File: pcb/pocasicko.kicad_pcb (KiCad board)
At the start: 2 copper layers, 100 x 88 mm, 65 parts, among them J1 SMA, J2 Header_SMD_1x05, J3 FPC24, J4 Header_SMD_1x03, Q1 AO3400A, SW1 SW_Push, SW2 A, SW3 B, SW4 C, SW5 D, U1 CMWX1ZZABZ-091, U2 BME680, U3 MP28200, U4 LM66100

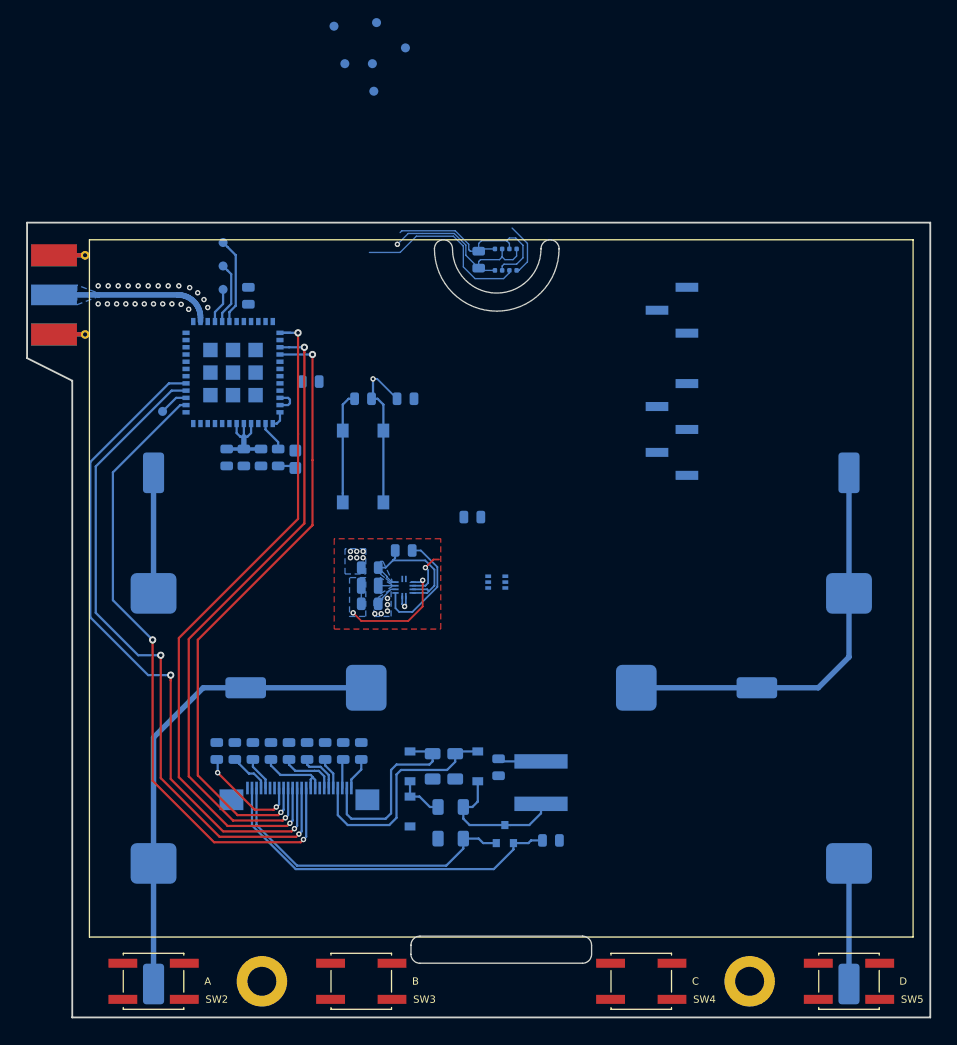
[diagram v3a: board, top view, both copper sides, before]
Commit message: Rotate the center cell diagonally
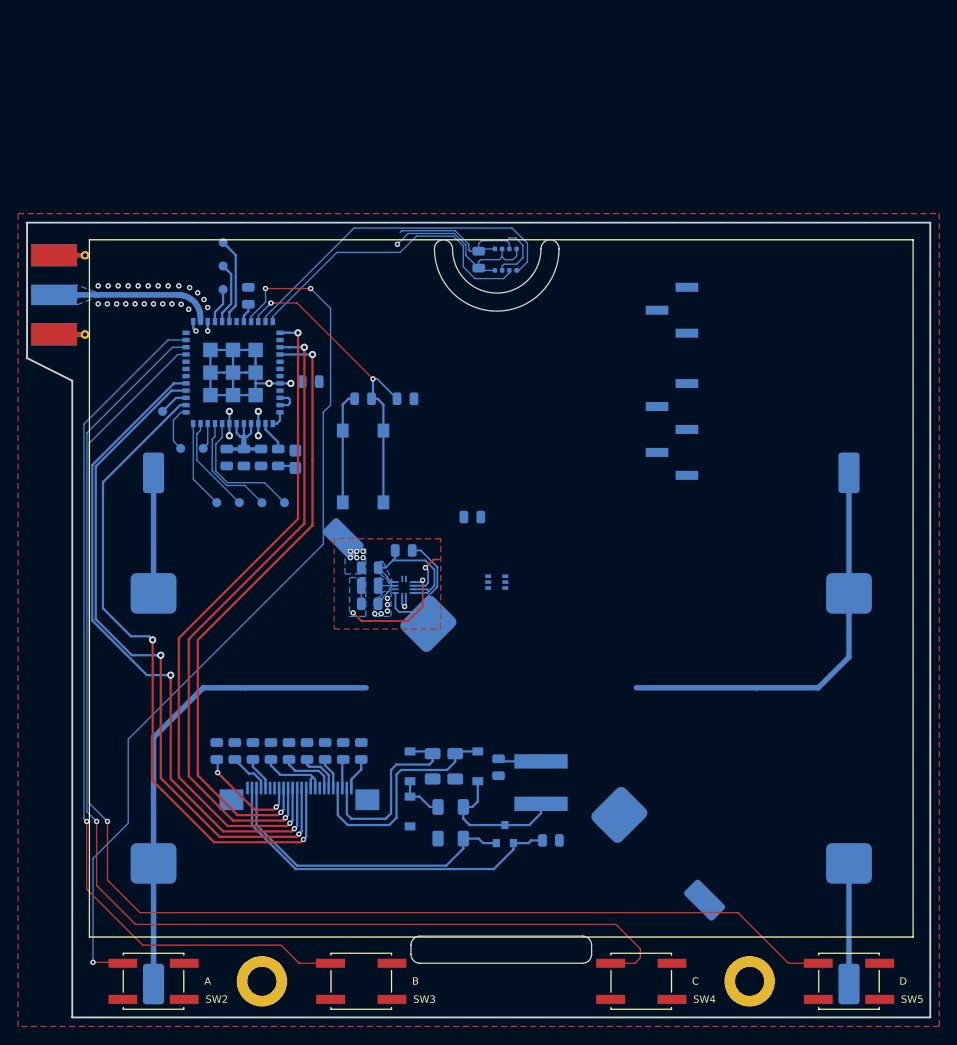
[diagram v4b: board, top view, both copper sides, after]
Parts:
- moved TP6 54.1 mm to (128.5, 81.0)
- moved TP9 53.6 mm to (123.5, 81.0)
- moved TP7 53.4 mm to (126.0, 81.0)
- moved TP5 48.8 mm to (121.0, 81.0)
- moved TP8 46.5 mm to (119.5, 75.0)
- moved TP4 46.3 mm to (117.0, 75.0)
- moved BT2 4.30 mm to (155.0, 105.0), turned to -45 degrees
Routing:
- net /BUTTON_D: track 0.00 -> 146.5 mm, vias 0 -> 1
- net /BUTTON_C: track 0.00 -> 133.1 mm, vias 0 -> 1
- net /BUTTON_A: track 0.00 -> 99.1 mm, vias 0 -> 3
- net /BUTTON_B: track 0.00 -> 97.2 mm, vias 0 -> 1
- net GND: track 51.7 -> 93.2 mm, vias 37 -> 42
- net /BME680_SCL: track 6.04 -> 37.9 mm
- net /~MCU_RESET: track 18.2 -> 35.7 mm, vias 1 -> 2
- net Net-(TP6-Pad1): track 0.00 -> 14.6 mm
- net /BME680_SDA: track 20.1 -> 34.3 mm
- net Net-(TP7-Pad1): track 0.00 -> 12.3 mm
- net Net-(TP9-Pad1): track 0.00 -> 10.9 mm
- net Net-(TP5-Pad1): track 0.00 -> 9.83 mm
- net Net-(TP4-Pad1): track 0.00 -> 5.23 mm
- net Net-(TP8-Pad1): track 0.00 -> 2.96 mm
- net +2V5: track 62.6 -> 64.7 mm
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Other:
- board text added: "Bačísek"
- board text added: "Chookity!"
- board text added: "Is it Tribore? Yes, it is!"

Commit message: Finished routing
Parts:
- added TP11: PA8, TestPoint:TestPoint_Pad_D1.0mm, B.Cu at (113.2, 67.5)
- added TP12: PH1, TestPoint:TestPoint_Pad_D1.0mm, B.Cu at (130.9, 70.1)
- added TP13: PB7, TestPoint:TestPoint_Pad_D1.0mm, B.Cu at (131.9, 62.6)
- SW1: value SW_Push -> RESET
- moved J4 22.0 mm to (168.3, 81.5)
- moved R7 9.93 mm to (146.1, 92.0), turned to 90 degrees
- moved J2 6.24 mm to (168.3, 67.5)
- moved BT2 5.59 mm to (152.5, 100.0), turned to 0 degrees
- moved U4 2.52 mm to (149.5, 89.5)
- moved U3 0.80 mm to (141.7, 89.6)
- moved C2 0.80 mm to (137.9, 87.4)
- moved C6 0.80 mm to (137.9, 91.4)
- moved L1 0.80 mm to (137.9, 89.4)
- moved R3 0.80 mm to (141.7, 85.5)
- moved R2 0.69 mm to (128.5, 76.0)
- moved D3 0.67 mm to (130.4, 76.2)
- moved R1 0.65 mm to (131.6, 67.0)
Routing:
- net +2V5: track 64.7 -> 232.8 mm, vias 2 -> 8
- net /USART1_TX: track 0.00 -> 100.3 mm, vias 0 -> 2
- net /USART1_RX: track 0.00 -> 94.9 mm, vias 0 -> 2
- net /BATT_VOLTAGE: track 17.2 -> 101.8 mm, vias 0 -> 2
- net GND: track 93.2 -> 154.7 mm, vias 42 -> 81
- net /SWDIO: track 0.00 -> 50.3 mm, vias 0 -> 2
- net Net-(BT3-Pad1): track 13.3 -> 58.9 mm
- net /SWCLK: track 0.00 -> 39.3 mm, vias 0 -> 2
- net /~MCU_RESET: track 35.7 -> 68.9 mm
- net /POWER_GOOD: track 13.4 -> 32.4 mm, vias 0 -> 2
- net /BUTTON_D: track 146.5 -> 154.4 mm
- net /BUTTON_A: track 99.1 -> 106.7 mm, vias 3 -> 5
- net /BUTTON_C: track 133.1 -> 140.7 mm
- net /BUTTON_B: track 97.2 -> 104.0 mm
- net Net-(TP11-Pad1): track 0.00 -> 5.27 mm
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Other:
- board text removed: "Bačísek"
- board text removed: "Chookity!"
- board text removed: "Is it Tribore? Yes, it is!"

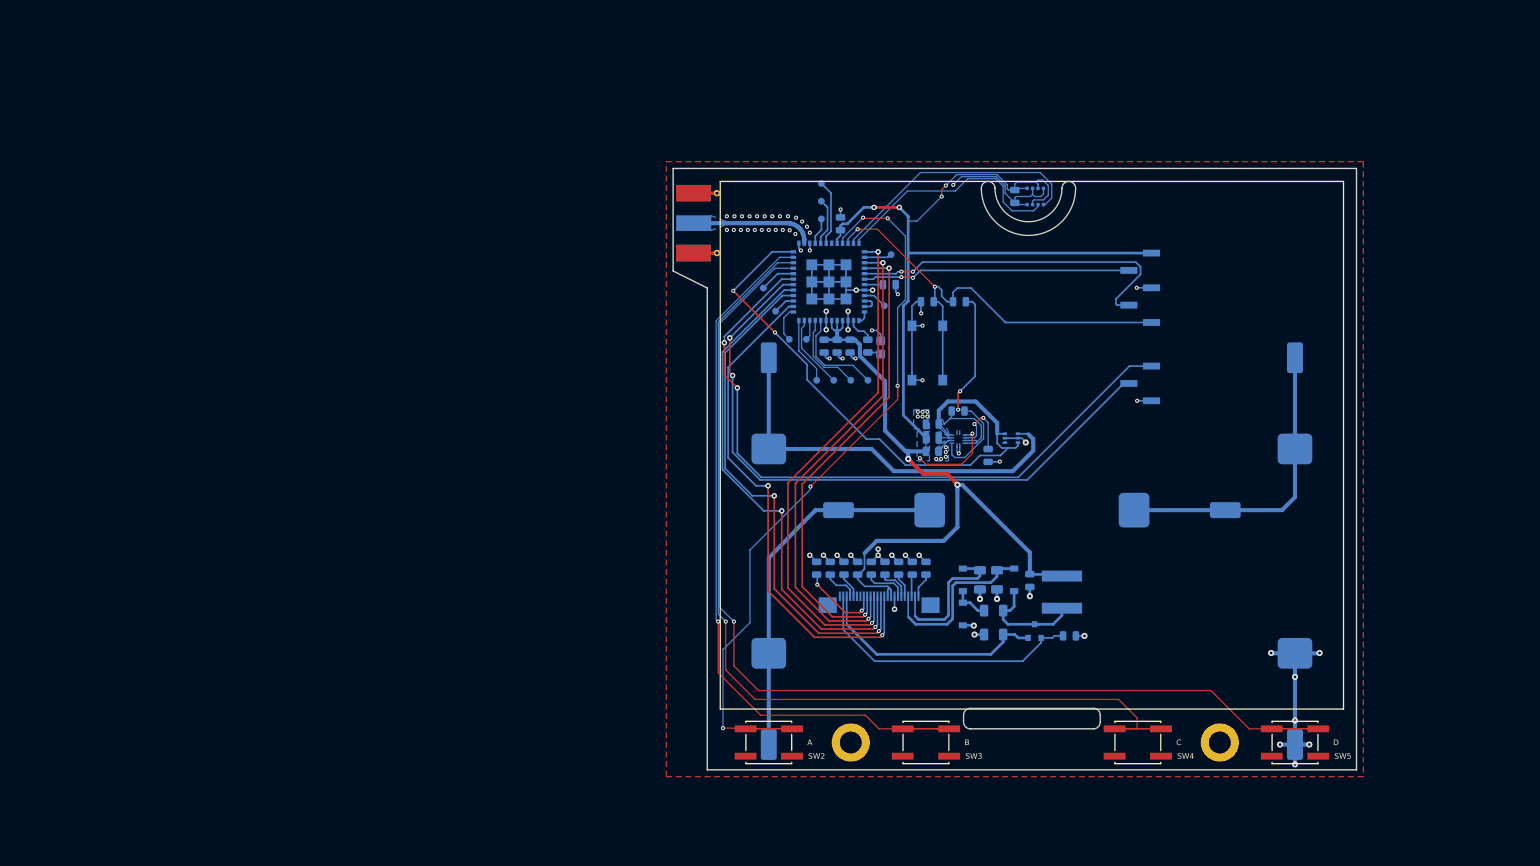
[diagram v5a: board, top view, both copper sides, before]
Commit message: Exchange SMA and add groundplane to the back layer
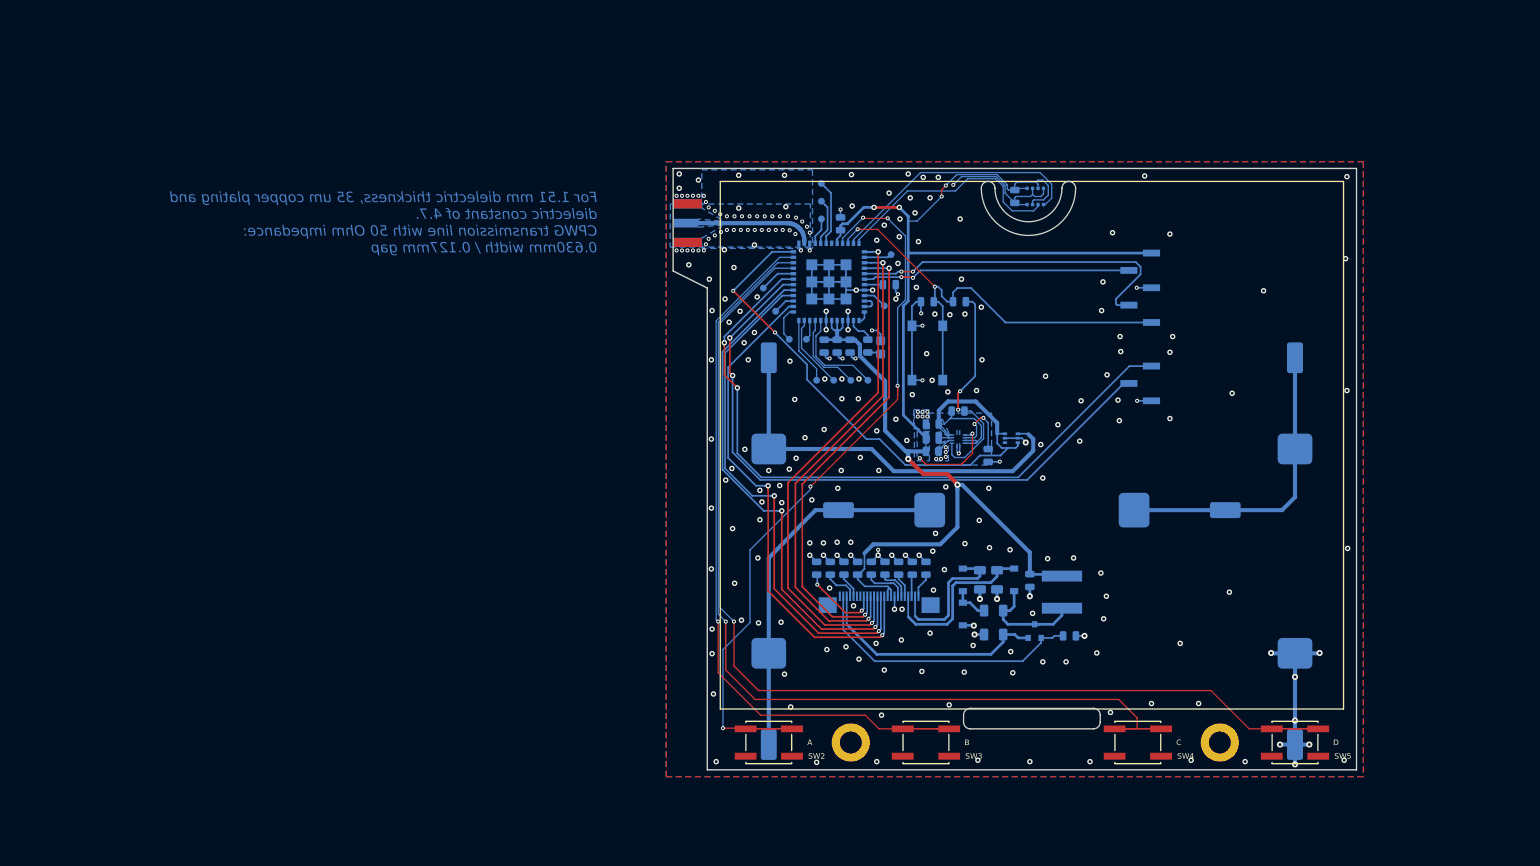
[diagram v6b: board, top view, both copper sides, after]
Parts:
- J1: footprint Connector_Coaxial:SMA_Molex_73251-1153_EdgeMount_Horizontal -> Connector_Coaxial:SMA_Samtec_SMA-J-P-H-ST-EM1_EdgeMount
- moved J1 2.60 mm to (102.1, 58.0), turned to 180 degrees
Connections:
- net /TSCL renamed Net-(J3-Pad6)
- net /TSDA renamed Net-(J3-Pad7)
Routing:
- net Net-(J1-Pad1): track 18.1 -> 20.5 mm
- net GND: vias 81 -> 272
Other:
- board text added: "For 1.51 mm dielectric thickness, 35 um copper plating and dielectric constant of 4.7. CPWG transmission line with 50 Ohm impedance: 0.630mm width / 0.127mm gap"

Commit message: Change BME interface from I2C to SPI
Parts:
- TP10: value PB14 -> PB9
- moved TP10 20.5 mm to (131.9, 59.3)
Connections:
- net /CS# renamed /DISP_NSS
- J3 pad 14: /SDI -> /MOSI
- U1 pad 14: /SDI -> /MOSI
- U1 pad 15: Net-(TP10-Pad1) -> /MISO
- U1 pad 35: /BME680_SCL -> /BME_NSS
- U1 pad 36: /BME680_SDA -> Net-(TP10-Pad1)
- U2 pad 2: +2V5 -> /BME_NSS
- U2 pad 3: /BME680_SDA -> /MOSI
- U2 pad 4: /BME680_SCL -> /SCLK
- U2 pad 5: GND -> /MISO
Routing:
- net /MOSI: track 0.00 -> 127.7 mm, vias 0 -> 4
- net /SDI: track 74.9 -> 0.00 mm, vias 2 -> 0
- net /SCLK: track 76.2 -> 148.8 mm, vias 2 -> 4
- net /BME_NSS: track 0.00 -> 59.1 mm
- net /MISO: track 0.00 -> 52.1 mm, vias 0 -> 2
- net /BME680_SCL: track 37.9 -> 0.00 mm
- net /BME680_SDA: track 34.3 -> 0.00 mm
- net +2V5: track 232.8 -> 225.9 mm
- net Net-(TP10-Pad1): track 3.22 -> 5.76 mm
- net GND: track 154.7 -> 152.5 mm, vias 272 -> 273
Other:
- board text added: "Chookity!"
